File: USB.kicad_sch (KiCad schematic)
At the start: 7 parts, among them J1 USB4110GFA, U2 USBLC6-2SC6

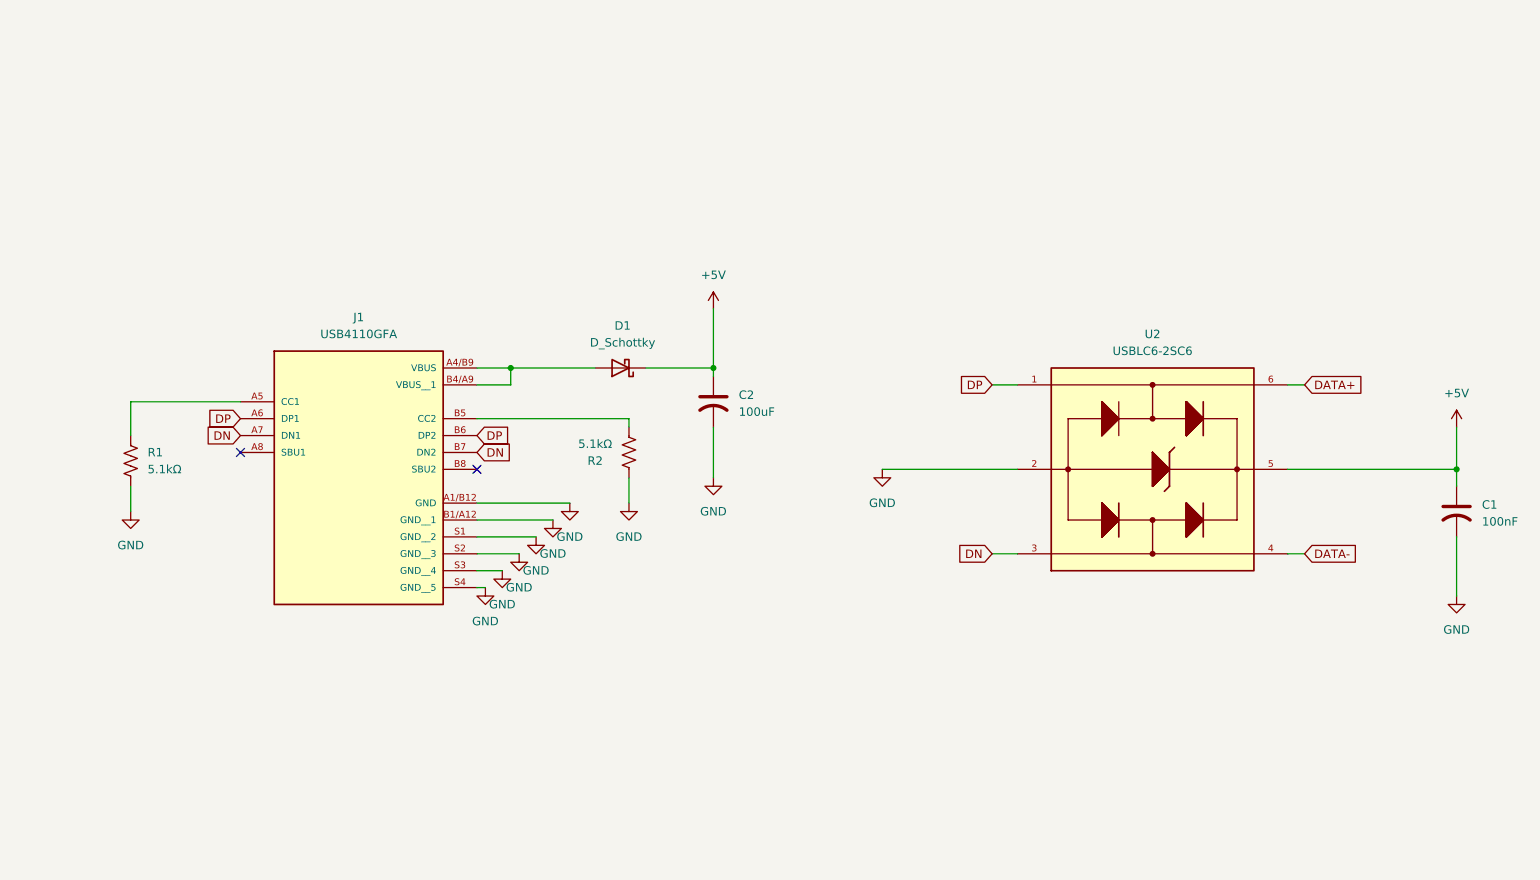
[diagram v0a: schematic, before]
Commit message: added power switch and RF module
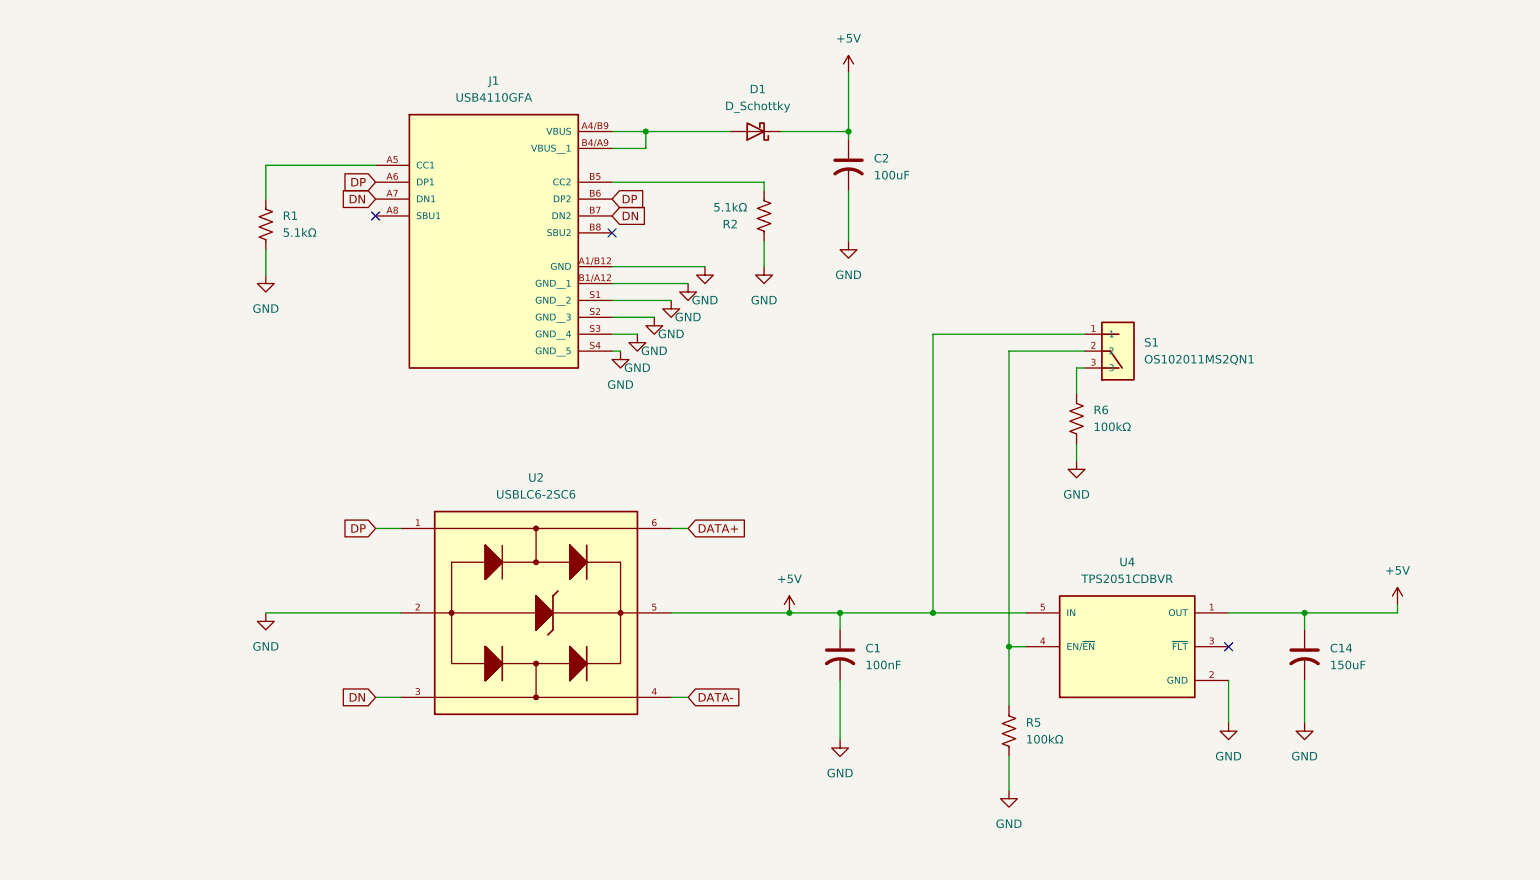
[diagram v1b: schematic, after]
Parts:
- added C14: 150uF, symbol Device:C_US
- added R5, R6: 100kΩ, symbol Device:R_US
- added S1: OS102011MS2QN1, OS102011MS2QN1:SW_OS102011MS2QN1, symbol OS102011MS2QN1:OS102011MS2QN1
- added U4: TPS2051CDBVR, TPS2051CDBVR:SOT95P280X145-5N, symbol TPS2051CDBVR:TPS2051CDBVR
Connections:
- net +5V: now also C14.1, S1.1, U4.1 (OUT), U4.5 (IN)
- net GND: now also C14.2, R5.2, R6.2, U4.2 (GND)
- new net: R5.1, S1.2, U4.4 (EN/~{EN})
- new net: R6.1, S1.3
- no-connect marks 2 -> 3
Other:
- moved on the sheet: C1, C2, D1, J1, R1, R2, U2

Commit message: Everything is done except for the programming pins
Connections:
- net +5V: no longer C1.1, C2.1, D1.1 (K), S1.1, U2.5, U4.5 (IN)
- new net: C1.1, C2.1, D1.1 (K), S1.1, U2.5, U4.5 (IN)
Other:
- moved on the sheet: C1, C14, C2, D1, J1, R1, R2, R5, R6, S1, U2, U4

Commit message: Edits
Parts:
- C2: footprint (none) -> Capacitor_SMD:C_01005_0402Metric
- C3: renamed from C1; footprint (none) -> Capacitor_SMD:C_01005_0402Metric
- C4: renamed from C14; footprint (none) -> Capacitor_SMD:C_01005_0402Metric
- R2: renamed from R1; footprint (none) -> Resistor_SMD:R_0402_1005Metric
- R4: renamed from R5; footprint (none) -> Resistor_SMD:R_0402_1005Metric
- R5: renamed from R6; footprint (none) -> Resistor_SMD:R_0402_1005Metric
- renumbered D1 to D2, J1 to J2, R2 to R3, S1 to S2, U4 to U3
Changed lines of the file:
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@@
 		(dnp no)
 		(fields_autoplaced yes)
-		(property "Reference" "#PWR036"
+		(property "Reference" "#PWR013"
 			(at 171.45 156.21 0)
 			(effects
@@
 			(project ""
 				(path "/bcf3418e-986f-42d9-beb5-94c6e2a384e4/5d432ce9-b304-44e3-a978-8be91b79b0ed"
-					(reference "#PWR036")
+					(reference "#PWR013")
 					(unit 1)
 				)
@@
 		(dnp no)
 		(fields_autoplaced yes)
-		(property "Reference" "R5"
+		(property "Reference" "R4"
 			(at 173.99 139.6999 0)
 			(effects
@@
 			)
 		)
-		(property "Footprint" ""
+		(property "Footprint" "Resistor_SMD:R_0402_1005Metric"
 			(at 172.466 141.224 90)
 			(effects
@@
 			(project ""
 				(path "/bcf3418e-986f-42d9-beb5-94c6e2a384e4/5d432ce9-b304-44e3-a978-8be91b79b0ed"
-					(reference "R5")
+					(reference "R4")
 					(unit 1)
 				)
@@
 		(dnp no)
 		(fields_autoplaced yes)
-		(property "Reference" "R1"
+		(property "Reference" "R2"
 			(at 35.56 54.6099 0)
 			(effects
@@
 			)
 		)
-		(property "Footprint" ""
+		(property "Footprint" "Resistor_SMD:R_0402_1005Metric"
 			(at 34.036 56.134 90)
 			(effects
@@
 			(project ""
 				(path "/bcf3418e-986f-42d9-beb5-94c6e2a384e4/5d432ce9-b304-44e3-a978-8be91b79b0ed"
-					(reference "R1")
+					(reference "R2")
 					(unit 1)
 				)
@@
 		(dnp no)
 		(fields_autoplaced yes)
-		(property "Reference" "D1"
+		(property "Reference" "D2"
 			(at 110.8075 35.56 0)
 			(effects
@@
 			(project ""
 				(path "/bcf3418e-986f-42d9-beb5-94c6e2a384e4/5d432ce9-b304-44e3-a978-8be91b79b0ed"
-					(reference "D1")
+					(reference "D2")
 					(unit 1)
 				)
@@
 		(dnp no)
 		(fields_autoplaced yes)
-		(property "Reference" "#PWR04"
+		(property "Reference" "#PWR09"
 			(at 99.06 68.58 0)
 			(effects
@@
 			(project "final_project"
 				(path "/bcf3418e-986f-42d9-beb5-94c6e2a384e4/5d432ce9-b304-44e3-a978-8be91b79b0ed"
-					(reference "#PWR04")
+					(reference "#PWR09")
 					(unit 1)
 				)
@@
 		(dnp no)
 		(fields_autoplaced yes)
-		(property "Reference" "#PWR035"
+		(property "Reference" "#PWR015"
 			(at 204.47 146.05 0)
 			(effects
@@
 			(project ""
 				(path "/bcf3418e-986f-42d9-beb5-94c6e2a384e4/5d432ce9-b304-44e3-a978-8be91b79b0ed"
-					(reference "#PWR035")
+					(reference "#PWR015")
 					(unit 1)
 				)
@@
 		(on_board yes)
 		(dnp no)
-		(property "Reference" "R6"
+		(property "Reference" "R5"
 			(at 184.15 92.7099 0)
 			(effects
@@
 			)
 		)
-		(property "Footprint" ""
+		(property "Footprint" "Resistor_SMD:R_0402_1005Metric"
 			(at 182.626 94.234 90)
 			(effects
@@
 			(project "final_project"
 				(path "/bcf3418e-986f-42d9-beb5-94c6e2a384e4/5d432ce9-b304-44e3-a978-8be91b79b0ed"
-					(reference "R6")
+					(reference "R5")
 					(unit 1)
 				)
@@
 		(on_board yes)
 		(dnp no)
-		(property "Reference" "R2"
+		(property "Reference" "R3"
 			(at 102.87 55.88 0)
 			(effects
@@
 			(project "final_project"
 				(path "/bcf3418e-986f-42d9-beb5-94c6e2a384e4/5d432ce9-b304-44e3-a978-8be91b79b0ed"
-					(reference "R2")
+					(reference "R3")
 					(unit 1)
 				)
@@
 		(dnp no)
 		(fields_autoplaced yes)
-		(property "Reference" "#PWR034"
+		(property "Reference" "#PWR016"
 			(at 215.9 146.05 0)
 			(effects
@@
 			(project ""
 				(path "/bcf3418e-986f-42d9-beb5-94c6e2a384e4/5d432ce9-b304-44e3-a978-8be91b79b0ed"
-					(reference "#PWR034")
+					(reference "#PWR016")
 					(unit 1)
 				)
@@
 		(dnp no)
 		(fields_autoplaced yes)
-		(property "Reference" "#PWR03"
+		(property "Reference" "#PWR011"
 			(at 120.65 64.77 0)
 			(effects
@@
 			(project "final_project"
 				(path "/bcf3418e-986f-42d9-beb5-94c6e2a384e4/5d432ce9-b304-44e3-a978-8be91b79b0ed"
-					(reference "#PWR03")
+					(reference "#PWR011")
 					(unit 1)
 				)
@@
 		(on_board yes)
 		(dnp no)
-		(property "Reference" "J1"
+		(property "Reference" "J2"
 			(at 67.31 34.29 0)
 			(effects
@@
 			(project "final_project"
 				(path "/bcf3418e-986f-42d9-beb5-94c6e2a384e4/5d432ce9-b304-44e3-a978-8be91b79b0ed"
-					(reference "J1")
+					(reference "J2")
 					(unit 1)
 				)
@@
 		(dnp no)
 		(fields_autoplaced yes)
-		(property "Reference" "U4"
+		(property "Reference" "U3"
 			(at 189.23 115.57 0)
 			(effects
@@
 			(project ""
 				(path "/bcf3418e-986f-42d9-beb5-94c6e2a384e4/5d432ce9-b304-44e3-a978-8be91b79b0ed"
-					(reference "U4")
+					(reference "U3")
 					(unit 1)
 				)
@@
 		(on_board yes)
 		(dnp no)
-		(property "Reference" "#PWR037"
+		(property "Reference" "#PWR014"
 			(at 181.61 106.68 0)
 			(effects
@@
 			(project "final_project"
 				(path "/bcf3418e-986f-42d9-beb5-94c6e2a384e4/5d432ce9-b304-44e3-a978-8be91b79b0ed"
-					(reference "#PWR037")
+					(reference "#PWR014")
 					(unit 1)
 				)
@@
 		(dnp no)
 		(fields_autoplaced yes)
-		(property "Reference" "#PWR033"
+		(property "Reference" "#PWR017"
 			(at 231.14 119.38 0)
 			(effects
@@
 			(project ""
 				(path "/bcf3418e-986f-42d9-beb5-94c6e2a384e4/5d432ce9-b304-44e3-a978-8be91b79b0ed"
-					(reference "#PWR033")
+					(reference "#PWR017")
 					(unit 1)
 				)
@@
 		(dnp no)
 		(fields_autoplaced yes)
-		(property "Reference" "#PWR05"
+		(property "Reference" "#PWR08"
 			(at 96.52 71.12 0)
 			(effects
@@
 			(project "final_project"
 				(path "/bcf3418e-986f-42d9-beb5-94c6e2a384e4/5d432ce9-b304-44e3-a978-8be91b79b0ed"
-					(reference "#PWR05")
+					(reference "#PWR08")
 					(unit 1)
 				)
@@
 		(dnp no)
 		(fields_autoplaced yes)
-		(property "Reference" "#PWR08"
+		(property "Reference" "#PWR05"
 			(at 88.9 78.74 0)
 			(effects
@@
 			(project "final_project"
 				(path "/bcf3418e-986f-42d9-beb5-94c6e2a384e4/5d432ce9-b304-44e3-a978-8be91b79b0ed"
-					(reference "#PWR08")
+					(reference "#PWR05")
 					(unit 1)
 				)
@@
 			)
 		)
-		(property "Footprint" ""
+		(property "Footprint" "Capacitor_SMD:C_01005_0402Metric"
 			(at 120.65 46.99 0)
 			(effects
@@
 		(dnp no)
 		(fields_autoplaced yes)
-		(property "Reference" "#PWR06"
+		(property "Reference" "#PWR07"
 			(at 93.98 73.66 0)
 			(effects
@@
 			(project "final_project"
 				(path "/bcf3418e-986f-42d9-beb5-94c6e2a384e4/5d432ce9-b304-44e3-a978-8be91b79b0ed"
-					(reference "#PWR06")
+					(reference "#PWR07")
 					(unit 1)
 				)
@@
 		(dnp no)
 		(fields_autoplaced yes)
-		(property "Reference" "#PWR012"
+		(property "Reference" "#PWR03"
 			(at 59.69 129.54 0)
 			(effects
@@
 			(project ""
 				(path "/bcf3418e-986f-42d9-beb5-94c6e2a384e4/5d432ce9-b304-44e3-a978-8be91b79b0ed"
-					(reference "#PWR012")
+					(reference "#PWR03")
 					(unit 1)
 				)
@@
 		(dnp no)
 		(fields_autoplaced yes)
-		(property "Reference" "C1"
+		(property "Reference" "C3"
 			(at 149.86 128.5239 0)
 			(effects
@@
 			)
 		)
-		(property "Footprint" ""
+		(property "Footprint" "Capacitor_SMD:C_01005_0402Metric"
 			(at 146.05 129.54 0)
 			(effects
@@
 			(project ""
 				(path "/bcf3418e-986f-42d9-beb5-94c6e2a384e4/5d432ce9-b304-44e3-a978-8be91b79b0ed"
-					(reference "C1")
+					(reference "C3")
 					(unit 1)
 				)
@@
 		(dnp no)
 		(fields_autoplaced yes)
-		(property "Reference" "#PWR07"
+		(property "Reference" "#PWR06"
 			(at 91.44 76.2 0)
 			(effects
@@
 			(project "final_project"
 				(path "/bcf3418e-986f-42d9-beb5-94c6e2a384e4/5d432ce9-b304-44e3-a978-8be91b79b0ed"
-					(reference "#PWR07")
+					(reference "#PWR06")
 					(unit 1)
 				)
@@
 		(dnp no)
 		(fields_autoplaced yes)
-		(property "Reference" "#PWR01"
+		(property "Reference" "#PWR02"
 			(at 33.02 69.85 0)
 			(effects
@@
 			(project ""
 				(path "/bcf3418e-986f-42d9-beb5-94c6e2a384e4/5d432ce9-b304-44e3-a978-8be91b79b0ed"
-					(reference "#PWR01")
+					(reference "#PWR02")
 					(unit 1)
 				)
@@
 		(dnp no)
 		(fields_autoplaced yes)
-		(property "Reference" "#PWR013"
+		(property "Reference" "#PWR010"
 			(at 107.95 68.58 0)
 			(effects
@@
 			(project ""
 				(path "/bcf3418e-986f-42d9-beb5-94c6e2a384e4/5d432ce9-b304-44e3-a978-8be91b79b0ed"
-					(reference "#PWR013")
+					(reference "#PWR010")
 					(unit 1)
 				)
@@
 		(dnp no)
 		(fields_autoplaced yes)
-		(property "Reference" "C14"
+		(property "Reference" "C4"
 			(at 219.71 128.5239 0)
 			(effects
@@
 			)
 		)
-		(property "Footprint" ""
+		(property "Footprint" "Capacitor_SMD:C_01005_0402Metric"
 			(at 215.9 129.54 0)
 			(effects
@@
 			(project ""
 				(path "/bcf3418e-986f-42d9-beb5-94c6e2a384e4/5d432ce9-b304-44e3-a978-8be91b79b0ed"
-					(reference "C14")
+					(reference "C4")
 					(unit 1)
 				)
@@
 		(dnp no)
 		(fields_autoplaced yes)
-		(property "Reference" "#FLG03"
+		(property "Reference" "#FLG02"
 			(at 97.79 40.005 0)
 			(effects
@@
 			(project ""
 				(path "/bcf3418e-986f-42d9-beb5-94c6e2a384e4/5d432ce9-b304-44e3-a978-8be91b79b0ed"
-					(reference "#FLG03")
+					(reference "#FLG02")
 					(unit 1)
 				)
@@
 		(dnp no)
 		(fields_autoplaced yes)
-		(property "Reference" "#PWR011"
+		(property "Reference" "#PWR012"
 			(at 146.05 148.59 0)
 			(effects
@@
 			(project ""
 				(path "/bcf3418e-986f-42d9-beb5-94c6e2a384e4/5d432ce9-b304-44e3-a978-8be91b79b0ed"
-					(reference "#PWR011")
+					(reference "#PWR012")
 					(unit 1)
 				)
@@
 		(dnp no)
 		(fields_autoplaced yes)
-		(property "Reference" "#PWR09"
+		(property "Reference" "#PWR04"
 			(at 86.36 81.28 0)
 			(effects
@@
 			(project "final_project"
 				(path "/bcf3418e-986f-42d9-beb5-94c6e2a384e4/5d432ce9-b304-44e3-a978-8be91b79b0ed"
-					(reference "#PWR09")
+					(reference "#PWR04")
 					(unit 1)
 				)
@@
 		(on_board yes)
 		(dnp no)
-		(property "Reference" "S1"
+		(property "Reference" "S2"
 			(at 191.77 82.5499 0)
 			(effects
@@
 			(project ""
 				(path "/bcf3418e-986f-42d9-beb5-94c6e2a384e4/5d432ce9-b304-44e3-a978-8be91b79b0ed"
-					(reference "S1")
-					(unit 1)
-				)
+					(reference "S2")
+					(unit 1)
+				)
